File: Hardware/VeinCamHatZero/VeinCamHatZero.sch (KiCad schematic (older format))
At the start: 22 parts, among them J1 Raspberry_Pi_2_3, Q1 BSD235N

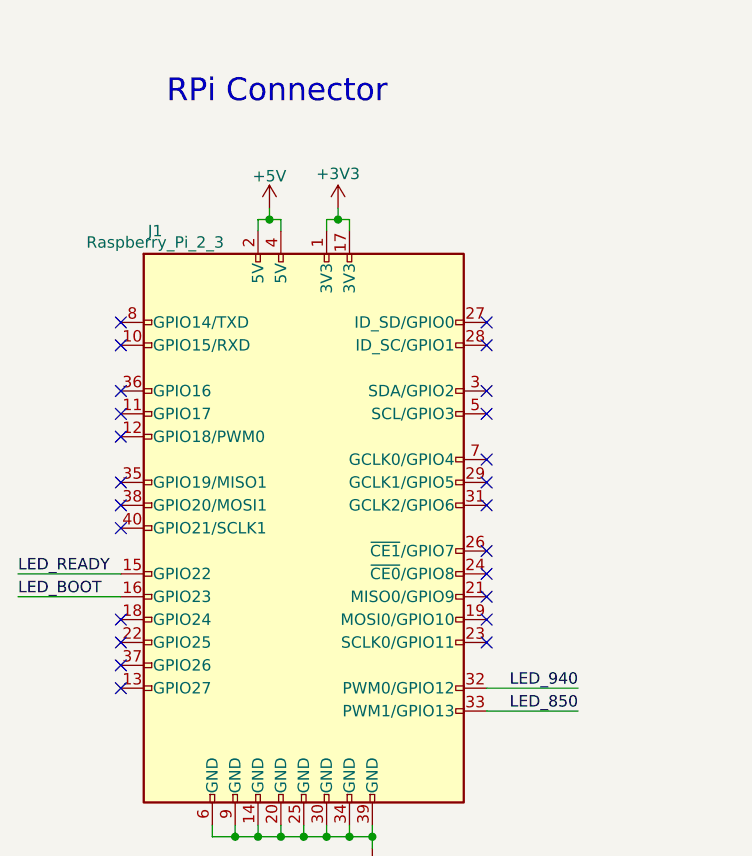
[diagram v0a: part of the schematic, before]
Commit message: Laid out VeinCamHatZero and added IR LED footprint/model
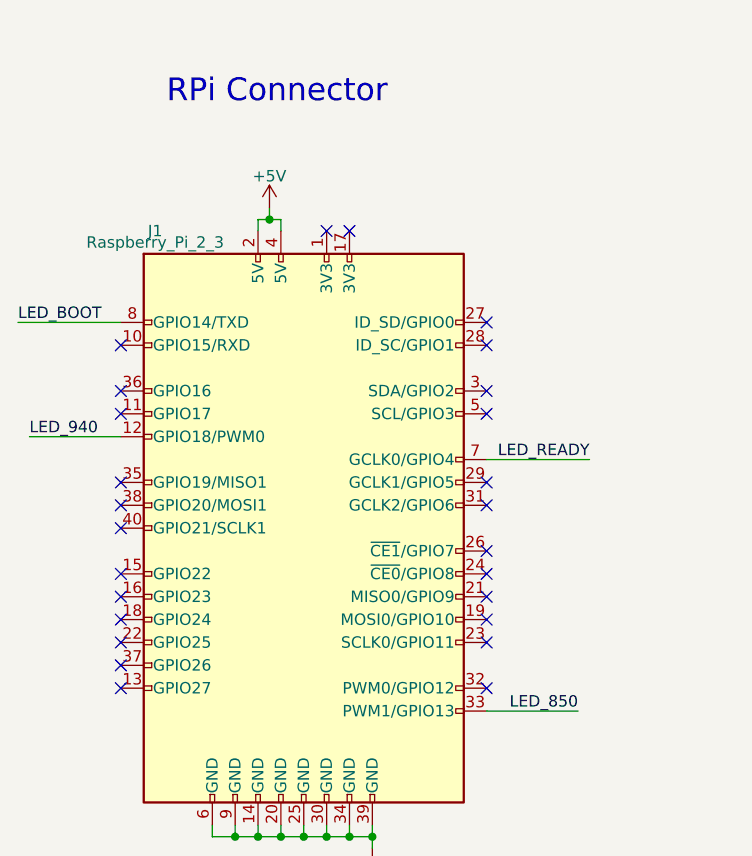
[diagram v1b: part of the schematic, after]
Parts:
- D1, D2, D3, D4, D6: footprint (none) -> VeinCam_Footprints:SFH7252
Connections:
- net +3V3: no longer J1.1 (3V3), J1.17 (3V3)
- net LED_940: now also J1.12 (GPIO18/PWM0); no longer J1.32 (PWM0/GPIO12)
- net LED_BOOT: now also J1.8 (GPIO14/TXD); no longer J1.16 (GPIO23)
- net LED_READY: now also J1.7 (GCLK0/GPIO4); no longer J1.15 (GPIO22)
- no-connect marks 26 -> 28
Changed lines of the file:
@@
 	6700 4050 6650 4050
 Wire Wire Line
-	3550 3650 3950 3650
-Wire Wire Line
 	3550 3750 3950 3750
-Text Label 3950 3650 2    50   ~ 0
-LED_940
 Text Label 3950 3750 2    50   ~ 0
 LED_850
@@
 	10450 2650 10450 3050
 Connection ~ 10450 2650
-Text Label 1500 3150 0    50   ~ 0
+Text Label 4000 2650 2    50   ~ 0
 LED_READY
 Wire Wire Line
-	1500 3150 1950 3150
-Wire Wire Line
-	1500 3250 1950 3250
-Text Label 1500 3250 0    50   ~ 0
+	4000 2650 3550 2650
+Wire Wire Line
+	1500 2050 1950 2050
+Text Label 1500 2050 0    50   ~ 0
 LED_BOOT
 Text Label 5900 4050 0    50   ~ 0
@@
 F 0 "D1" H 6600 2350 50  0000 C CNN
 F 1 "SFH7252" H 6600 1850 50  0000 C CNN
-F 2 "" H 6630 2100 50  0001 C CNN
+F 2 "VeinCam_Footprints:SFH7252" H 6630 2100 50  0001 C CNN
 F 3 "~" H 6630 2100 50  0001 C CNN
 	1    6600 2100
@@
 F 0 "D2" H 6600 3000 50  0000 C CNN
 F 1 "SFH7252" H 6600 2500 50  0000 C CNN
-F 2 "" H 6630 2750 50  0001 C CNN
+F 2 "VeinCam_Footprints:SFH7252" H 6630 2750 50  0001 C CNN
 F 3 "~" H 6630 2750 50  0001 C CNN
 	1    6600 2750
@@
 F 0 "D4" H 7550 3000 50  0000 C CNN
 F 1 "SFH7252" H 7550 2500 50  0000 C CNN
-F 2 "" H 7580 2750 50  0001 C CNN
+F 2 "VeinCam_Footprints:SFH7252" H 7580 2750 50  0001 C CNN
 F 3 "~" H 7580 2750 50  0001 C CNN
 	1    7550 2750
@@
 F 0 "D6" H 8500 3000 50  0000 C CNN
 F 1 "SFH7252" H 8500 2500 50  0000 C CNN
-F 2 "" H 8530 2750 50  0001 C CNN
+F 2 "VeinCam_Footprints:SFH7252" H 8530 2750 50  0001 C CNN
 F 3 "~" H 8530 2750 50  0001 C CNN
 	1    8500 2750
@@
 F 0 "D3" H 7550 2350 50  0000 C CNN
 F 1 "SFH7252" H 7550 1850 50  0000 C CNN
-F 2 "" H 7580 2100 50  0001 C CNN
+F 2 "VeinCam_Footprints:SFH7252" H 7580 2100 50  0001 C CNN
 F 3 "~" H 7580 2100 50  0001 C CNN
 	1    7550 2100
@@
 Wire Wire Line
 	2600 1600 2650 1600
-Wire Wire Line
-	2850 1650 2850 1600
-Wire Wire Line
-	2850 1600 2900 1600
-Wire Wire Line
-	2950 1600 2950 1650
-Wire Wire Line
-	2900 1600 2900 1550
-Connection ~ 2900 1600
-Wire Wire Line
-	2900 1600 2950 1600
-$Comp
-L power:+3V3 #PWR02
-U 1 1 5C92386C
-P 2900 1550
-F 0 "#PWR02" H 2900 1400 50  0001 C CNN
-F 1 "+3V3" H 2900 1700 50  0000 C CNN
-F 2 "" H 2900 1550 50  0001 C CNN
-F 3 "" H 2900 1550 50  0001 C CNN
-	1    2900 1550
-	1    0    0    -1
-$EndComp
-NoConn ~ 1950 2050
 NoConn ~ 1950 2150
 NoConn ~ 1950 2350
 NoConn ~ 1950 2450
-NoConn ~ 1950 2550
 NoConn ~ 1950 2750
 NoConn ~ 1950 2850
@@
 NoConn ~ 3550 2850
 NoConn ~ 3550 2750
-NoConn ~ 3550 2650
 NoConn ~ 3550 2450
 NoConn ~ 3550 2350
@@
 $EndComp
 NoConn ~ 4750 7000
+Wire Wire Line
+	1950 2550 1550 2550
+Text Label 1550 2550 0    50   ~ 0
+LED_940
+NoConn ~ 3550 3650
+NoConn ~ 1950 3150
+NoConn ~ 1950 3250
+NoConn ~ 2850 1650
+NoConn ~ 2950 1650
 $EndSCHEMATC

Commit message: More Hardware changes, both boards complete
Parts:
- removed Q1: BSD235N, Package_TO_SOT_SMD:SOT-363_SC-70-6, symbol VeinCam_Symbols:BSD235N
- added Q1: NTJD4001N, Package_TO_SOT_SMD:SOT-363_SC-70-6, symbol VeinCam_Symbols:NTJD4001N
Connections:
- net GND: now also Q1.1 (S), Q1.4 (S)
- net LED_850: now also Q1.5 (G)
- net LED_940: now also Q1.2 (G)
- net at D3.3 (K1), D6.3 (K1): now also Q1.6 (D)
- net at D3.1 (K2), D6.1 (K2): now also Q1.3 (D)
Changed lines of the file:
@@
 	7000 4500 7250 4500
-$Comp
-L VeinCam_Symbols:BSD235N Q1
-U 1 1 5C89B330
-P 8900 3250
-F 0 "Q1" H 9106 3296 50  0000 L CNN
-F 1 "BSD235N" H 9106 3205 50  0000 L CNN
-F 2 "Package_TO_SOT_SMD:SOT-363_SC-70-6" H 9100 3250 50  0001 C CNN
-F 3 "~" H 9100 3250 50  0001 C CNN
-	1    8900 3250
-	1    0    0    -1
-$EndComp
-$Comp
-L VeinCam_Symbols:BSD235N Q1
-U 2 1 5C89B4BB
-P 10350 3250
-F 0 "Q1" H 10556 3296 50  0000 L CNN
-F 1 "BSD235N" H 10556 3205 50  0000 L CNN
-F 2 "Package_TO_SOT_SMD:SOT-363_SC-70-6" H 10550 3250 50  0001 C CNN
-F 3 "~" H 10550 3250 50  0001 C CNN
-	2    10350 3250
-	1    0    0    -1
-$EndComp
 $Comp
 L VeinCam_Symbols:SFH7252 D1
@@
 NoConn ~ 2850 1650
 NoConn ~ 2950 1650
+$Comp
+L VeinCam_Symbols:NTJD4001N Q1
+U 1 1 5C92154C
+P 8900 3250
+F 0 "Q1" H 9106 3296 50  0000 L CNN
+F 1 "NTJD4001N" H 9106 3205 50  0000 L CNN
+F 2 "Package_TO_SOT_SMD:SOT-363_SC-70-6" H 9100 3250 50  0001 C CNN
+F 3 "~" H 9100 3250 50  0001 C CNN
+	1    8900 3250
+	1    0    0    -1
+$EndComp
+$Comp
+L VeinCam_Symbols:NTJD4001N Q1
+U 2 1 5C9215DD
+P 10350 3250
+F 0 "Q1" H 10556 3296 50  0000 L CNN
+F 1 "NTJD4001N" H 10556 3205 50  0000 L CNN
+F 2 "Package_TO_SOT_SMD:SOT-363_SC-70-6" H 10550 3250 50  0001 C CNN
+F 3 "~" H 10550 3250 50  0001 C CNN
+	2    10350 3250
+	1    0    0    -1
+$EndComp
 $EndSCHEMATC
